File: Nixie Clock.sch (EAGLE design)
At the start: 136 parts, among them IC1_SECONDS_UNITS 4017N, IC2_SECONDS_TENS 4017N, IC3_MINUTES_UNITS 4017N, IC4_MINUTES_TENS 4017N, IC5_HOURS_UNITS 4017N, IC6_HOURS_TENS 4017N, T0 MPSA42, T1 MPSA42, T10 MPSA42, T11 MPSA42, T12 MPSA42, T13 MPSA42, T14 MPSA42, T15 MPSA42, T16 MPSA42, T17 MPSA42, T18 MPSA42, T19 MPSA42, T2 MPSA42, T20 MPSA42, T21 MPSA42, T22 MPSA42, T23 MPSA42, T24 MPSA42, T25 MPSA42, T26 MPSA42, T27 MPSA42, T28 MPSA42, T29 MPSA42, T3 MPSA42, T30 MPSA42, T31 MPSA42, T32 MPSA42, T33 MPSA42, T34 MPSA42, T35 MPSA42, T36 MPSA42, T37 MPSA42, T38 MPSA42, T39 MPSA42, T4 MPSA42, T40 MPSA42, T41 MPSA42, T42 MPSA42, T43 MPSA42, T44 MPSA42, T5 MPSA42, T6 MPSA42, T7 MPSA42, T8 MPSA42, T9 MPSA42

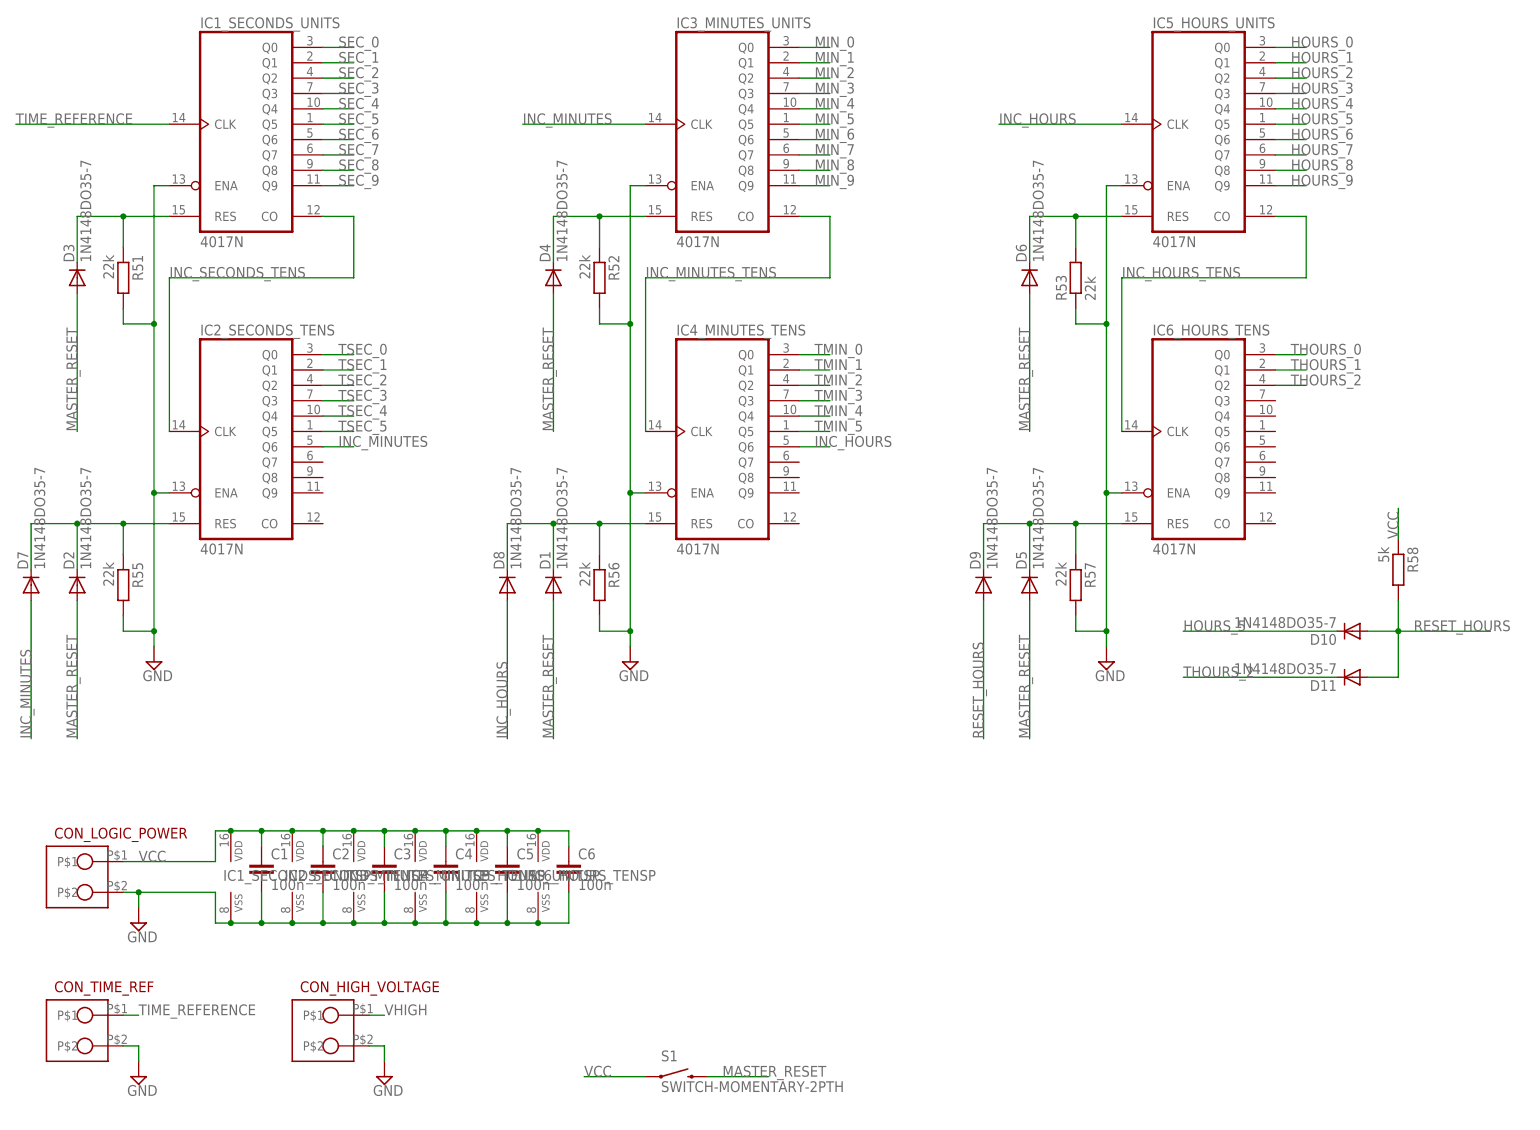
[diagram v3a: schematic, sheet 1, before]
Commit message: Complete schematics and finish placing components
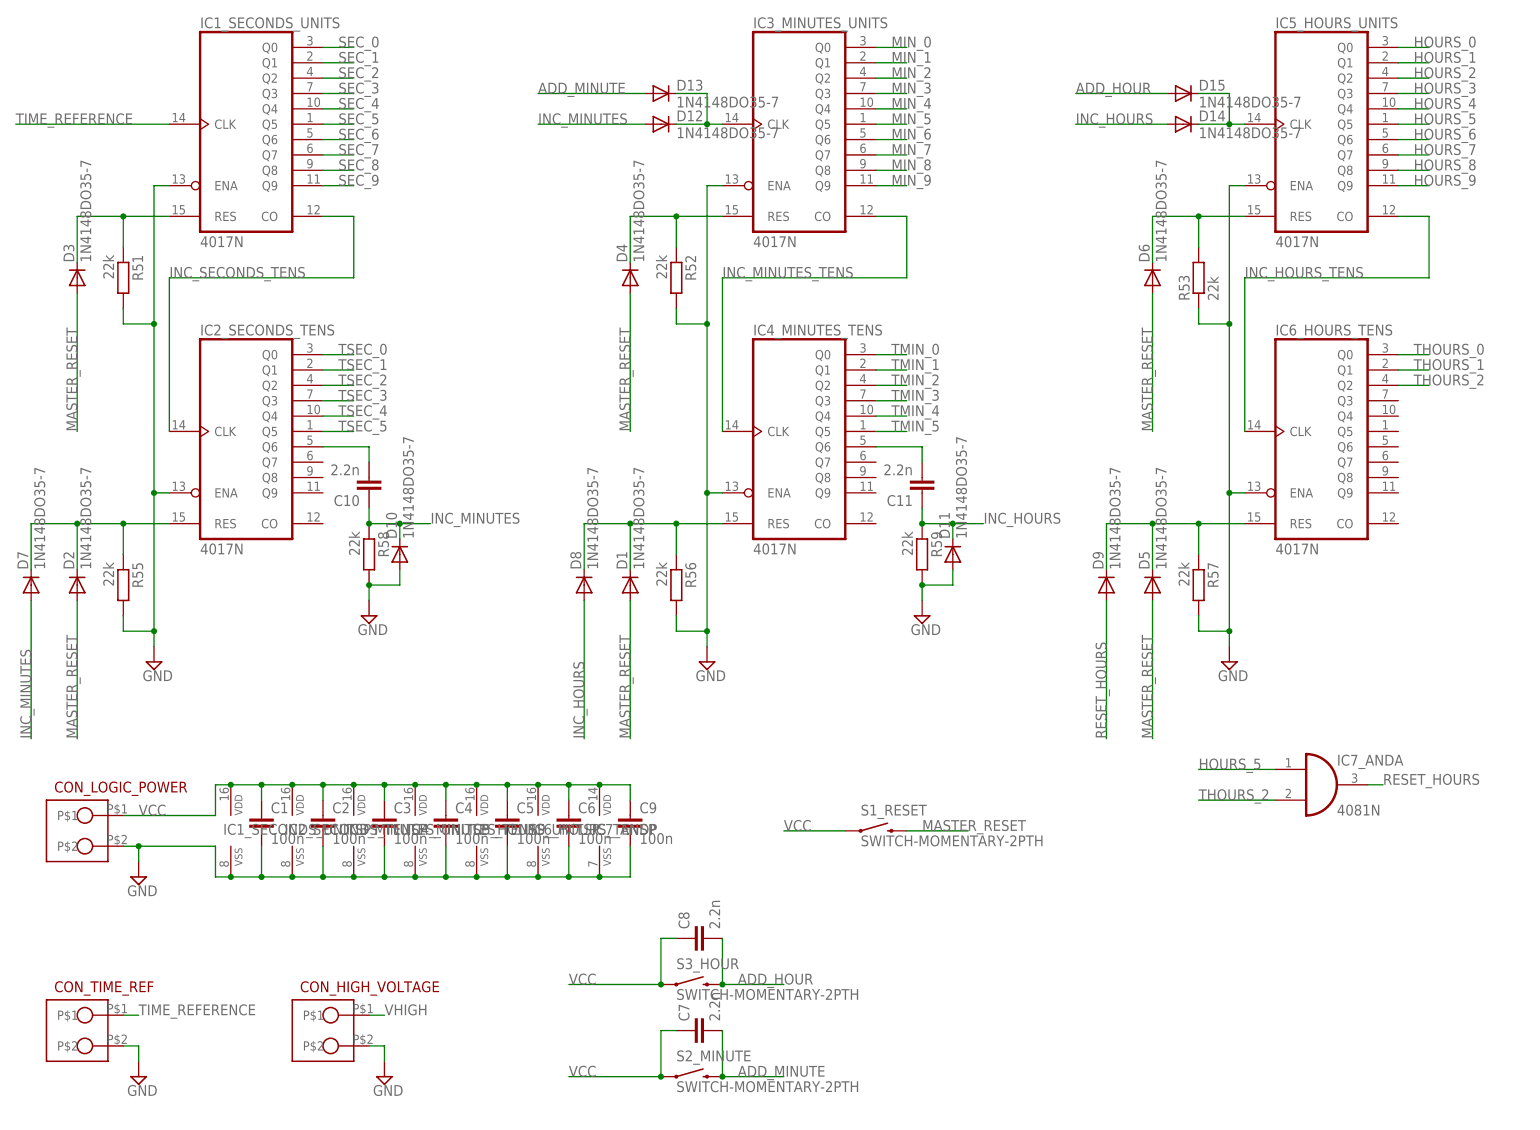
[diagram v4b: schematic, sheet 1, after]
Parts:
- removed S1: SWITCH-MOMENTARY-2PTH, SparkFun-Electromechanical:SWITCH-MOMENTARY-2PTH
- added C10, C11, C7, C8: 2.2n, resistor:C-EU050-030X075
- added C9: 100n, resistor:C-EU050-030X075
- added D12, D13, D14, D15: 1N4148DO35-7, diode:1N4148DO35-7
- added IC7_AND: 4081N, 40xx:4081N
- added R59: 22k, resistor:R-EU_0207/10
- added S1_RESET, S2_MINUTE, S3_HOUR: SWITCH-MOMENTARY-2PTH, SparkFun-Electromechanical:SWITCH-MOMENTARY-2PTH
- R1, R19, R2, R20, R37, R38: value (none) -> 10k
- R58: value 5k -> 22k
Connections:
- new net ADD_HOUR: C8.2, D15.A, S3_HOUR.2
- new net ADD_MINUTE: C7.2, D13.A, S2_MINUTE.2
- new net N$101: C11.2, IC4_MINUTES_TENSA.Q6
- new net N$103: D12.C, D13.C, IC3_MINUTES_UNITSA.CLK
- new net N$105: D14.C, D15.C, IC5_HOURS_UNITSA.CLK
- new net N$90: C10.2, IC2_SECONDS_TENSA.Q6
- net GND: now also C9.2, D10.A, D11.A, IC7_ANDP.VSS, R58.2, R59.2
- net HOURS_5: now also IC7_ANDA.I0; no longer D10.C
- net INC_HOURS: now also C11.1, D11.C, D14.A, R59.1; no longer IC4_MINUTES_TENSA.Q6, IC5_HOURS_UNITSA.CLK
- net INC_MINUTES: now also C10.1, D10.C, D12.A, R58.1; no longer IC2_SECONDS_TENSA.Q6, IC3_MINUTES_UNITSA.CLK
- net MASTER_RESET: now also S1_RESET.2; no longer S1.2
- net RESET_HOURS: now also IC7_ANDA.O; no longer D10.A, D11.A, R58.2
- net THOURS_2: now also IC7_ANDA.I1; no longer D11.C
- net VCC: now also C7.1, C8.1, C9.1, IC7_ANDP.VDD, S1_RESET.1, S2_MINUTE.1, S3_HOUR.1; no longer R58.1, S1.1
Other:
- moved on the sheet: C1, C2, C3, C4, C5, C6, CON_LOGIC_POWER, D1, D10, D11, D4, D5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

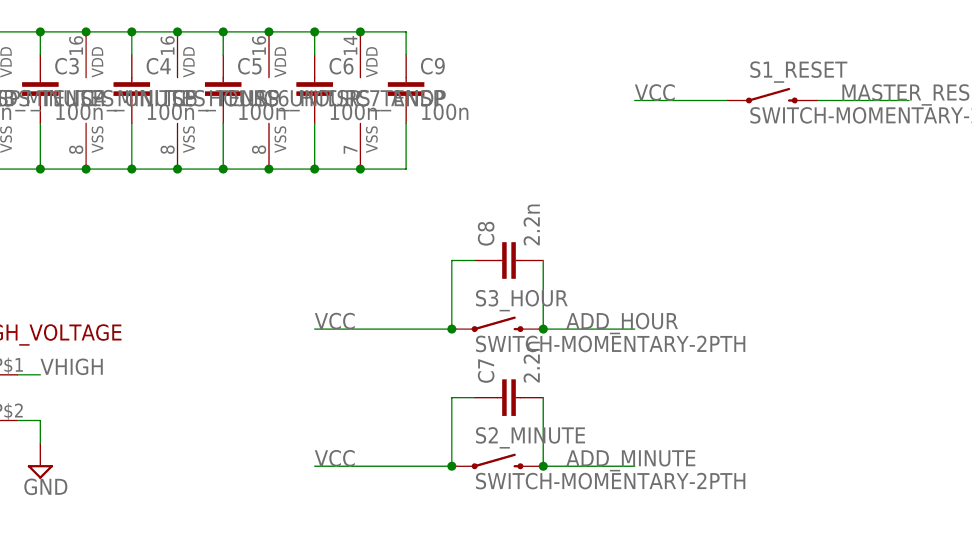
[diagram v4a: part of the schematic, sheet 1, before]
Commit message: Complete layout of control signals for 4017s
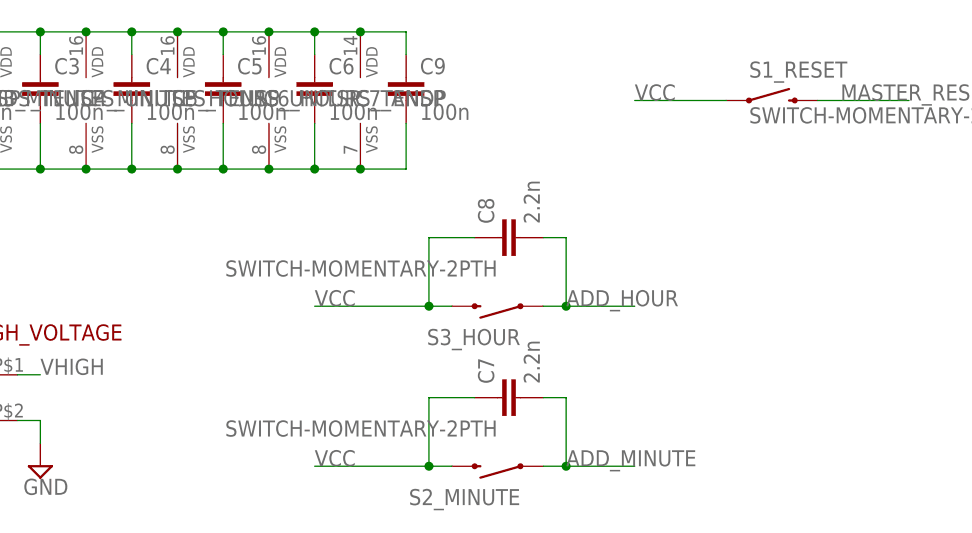
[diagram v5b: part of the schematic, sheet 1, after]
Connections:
- net ADD_HOUR: now also S3_HOUR.1; no longer S3_HOUR.2
- net ADD_MINUTE: now also S2_MINUTE.1; no longer S2_MINUTE.2
- net VCC: now also S2_MINUTE.2, S3_HOUR.2; no longer S2_MINUTE.1, S3_HOUR.1
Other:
- moved on the sheet: C8, S2_MINUTE, S3_HOUR
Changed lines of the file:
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@@
 <instance part="C5" gate="G$1" x="83.82" y="50.8"/>
 <instance part="C6" gate="G$1" x="93.98" y="50.8"/>
-<instance part="S2_MINUTE" gate="G$1" x="114.3" y="7.62"/>
-<instance part="S3_HOUR" gate="G$1" x="114.3" y="22.86"/>
+<instance part="S2_MINUTE" gate="G$1" x="114.3" y="7.62" smashed="yes" rot="R180">
+<attribute name="NAME" x="116.84" y="5.08" size="1.778" layer="95" rot="R180"/>
+<attribute name="VALUE" x="114.3" y="12.7" size="1.778" layer="96" rot="R180"/>
+</instance>
+<instance part="S3_HOUR" gate="G$1" x="114.3" y="25.4" smashed="yes" rot="R180">
+<attribute name="NAME" x="116.84" y="22.86" size="1.778" layer="95" rot="R180"/>
+<attribute name="VALUE" x="114.3" y="30.48" size="1.778" layer="96" rot="R180"/>
+</instance>
 <instance part="C7" gate="G$1" x="114.3" y="15.24" rot="R90"/>
-<instance part="C8" gate="G$1" x="114.3" y="30.48" rot="R90"/>
+<instance part="C8" gate="G$1" x="114.3" y="33.02" rot="R90"/>
 <instance part="IC7_AND" gate="A" x="218.44" y="55.88"/>
 <instance part="C9" gate="G$1" x="104.14" y="50.8"/>
@@
 <segment>
 <pinref part="C7" gate="G$1" pin="1"/>
-<pinref part="S2_MINUTE" gate="G$1" pin="1"/>
-<wire x1="111.76" y1="15.24" x2="109.22" y2="15.24" width="0.1524" layer="91"/>
-<wire x1="109.22" y1="15.24" x2="109.22" y2="7.62" width="0.1524" layer="91"/>
-<wire x1="93.98" y1="7.62" x2="109.22" y2="7.62" width="0.1524" layer="91"/>
-<junction x="109.22" y="7.62"/>
+<wire x1="93.98" y1="7.62" x2="106.68" y2="7.62" width="0.1524" layer="91"/>
 <label x="93.98" y="7.62" size="1.778" layer="95"/>
+<wire x1="111.76" y1="15.24" x2="106.68" y2="15.24" width="0.1524" layer="91"/>
+<wire x1="106.68" y1="15.24" x2="106.68" y2="7.62" width="0.1524" layer="91"/>
+<pinref part="S2_MINUTE" gate="G$1" pin="2"/>
+<wire x1="109.22" y1="7.62" x2="106.68" y2="7.62" width="0.1524" layer="91"/>
+<junction x="106.68" y="7.62"/>
 </segment>
 <segment>
 <pinref part="C8" gate="G$1" pin="1"/>
-<pinref part="S3_HOUR" gate="G$1" pin="1"/>
-<wire x1="111.76" y1="30.48" x2="109.22" y2="30.48" width="0.1524" layer="91"/>
-<wire x1="109.22" y1="30.48" x2="109.22" y2="22.86" width="0.1524" layer="91"/>
-<wire x1="93.98" y1="22.86" x2="109.22" y2="22.86" width="0.1524" layer="91"/>
-<junction x="109.22" y="22.86"/>
-<label x="93.98" y="22.86" size="1.778" layer="95"/>
+<wire x1="93.98" y1="25.4" x2="106.68" y2="25.4" width="0.1524" layer="91"/>
+<label x="93.98" y="25.4" size="1.778" layer="95"/>
+<wire x1="111.76" y1="33.02" x2="106.68" y2="33.02" width="0.1524" layer="91"/>
+<wire x1="106.68" y1="33.02" x2="106.68" y2="25.4" width="0.1524" layer="91"/>
+<pinref part="S3_HOUR" gate="G$1" pin="2"/>
+<wire x1="106.68" y1="25.4" x2="109.22" y2="25.4" width="0.1524" layer="91"/>
+<junction x="106.68" y="25.4"/>
 </segment>
 </net>
@@
 <net name="ADD_MINUTE" class="0">
 <segment>
-<pinref part="S2_MINUTE" gate="G$1" pin="2"/>
 <label x="121.92" y="7.62" size="1.778" layer="95"/>
-<wire x1="119.38" y1="7.62" x2="129.54" y2="7.62" width="0.1524" layer="91"/>
 <pinref part="C7" gate="G$1" pin="2"/>
-<wire x1="119.38" y1="7.62" x2="119.38" y2="15.24" width="0.1524" layer="91"/>
-<junction x="119.38" y="7.62"/>
+<wire x1="121.92" y1="7.62" x2="129.54" y2="7.62" width="0.1524" layer="91"/>
+<wire x1="119.38" y1="15.24" x2="121.92" y2="15.24" width="0.1524" layer="91"/>
+<wire x1="121.92" y1="15.24" x2="121.92" y2="7.62" width="0.1524" layer="91"/>
+<pinref part="S2_MINUTE" gate="G$1" pin="1"/>
+<wire x1="119.38" y1="7.62" x2="121.92" y2="7.62" width="0.1524" layer="91"/>
+<junction x="121.92" y="7.62"/>
 </segment>
 <segment>
@@
 <net name="ADD_HOUR" class="0">
 <segment>
-<pinref part="S3_HOUR" gate="G$1" pin="2"/>
-<wire x1="129.54" y1="22.86" x2="119.38" y2="22.86" width="0.1524" layer="91"/>
-<label x="121.92" y="22.86" size="1.778" layer="95"/>
+<wire x1="129.54" y1="25.4" x2="121.92" y2="25.4" width="0.1524" layer="91"/>
+<label x="121.92" y="25.4" size="1.778" layer="95"/>
 <pinref part="C8" gate="G$1" pin="2"/>
-<wire x1="119.38" y1="22.86" x2="119.38" y2="30.48" width="0.1524" layer="91"/>
-<junction x="119.38" y="22.86"/>
-</segment>
-<segment>
+<wire x1="119.38" y1="33.02" x2="121.92" y2="33.02" width="0.1524" layer="91"/>
+<wire x1="121.92" y1="33.02" x2="121.92" y2="25.4" width="0.1524" layer="91"/>
+<pinref part="S3_HOUR" gate="G$1" pin="1"/>
+<wire x1="119.38" y1="25.4" x2="121.92" y2="25.4" width="0.1524" layer="91"/>
+<junction x="121.92" y="25.4"/>
+</segment>
+<segment>
